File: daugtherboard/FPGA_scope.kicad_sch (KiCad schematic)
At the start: 21 parts, among them J3 HDMI_A, U1 OV5640, U2 TLV71315PDBV, U3 TLV71328PDBV

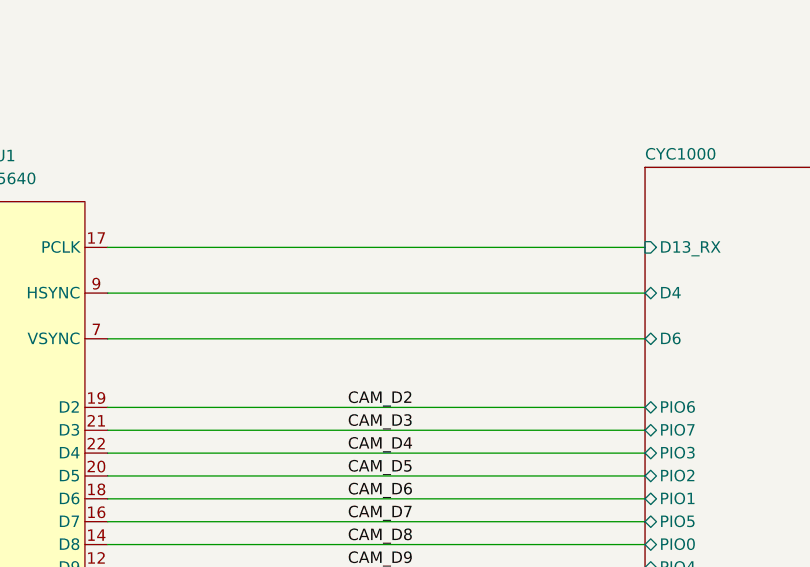
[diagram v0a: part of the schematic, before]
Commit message: start of PC Software
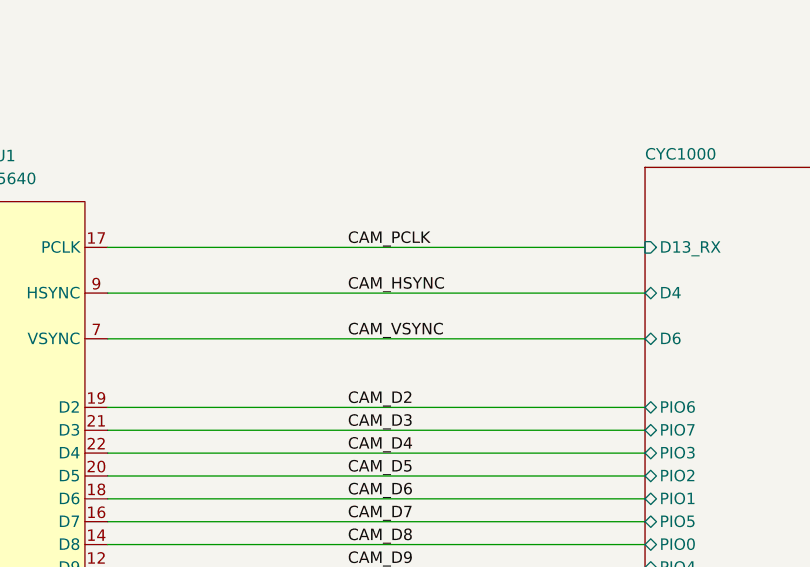
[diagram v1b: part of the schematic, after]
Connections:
- net CYC1000/D13_RX renamed CAM_PCLK
- net CYC1000/D4 renamed CAM_HSYNC
- net CYC1000/D6 renamed CAM_VSYNC
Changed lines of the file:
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@@
+		)
+	)
+	(label "CAM_PCLK"
+		(at 101.6 59.69 0)
+		(effects
+			(font
+				(size 1.27 1.27)
+			)
+			(justify left bottom)
 		)
 	)
@@
 		)
 	)
+	(label "CAM_VSYNC"
+		(at 101.6 69.85 0)
+		(effects
+			(font
+				(size 1.27 1.27)
+			)
+			(justify left bottom)
+		)
+	)
 	(label "CAM_D6"
 		(at 101.6 87.63 0)
@@
 		(effects
 			(font
+				(size 1.27 1.27)
+			)
+			(justify left bottom)
+		)
+	)
+	(label "CAM_HSYNC"
+		(at 101.6 64.77 0)
+		(effects
+			(font
